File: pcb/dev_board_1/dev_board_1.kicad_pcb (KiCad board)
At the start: 2 copper layers, 90 x 97.5 mm, 54 parts, among them SW1 SW_DIP_x01, SW10 SW_DIP_x01, SW11 SW_DIP_x01, SW12 SW_DIP_x01, SW13 SW_DIP_x01, SW14 SW_DIP_x01, SW15 SW_DIP_x01, SW16 SW_DIP_x01, SW17 SW_DIP_x01, SW18 SW_DIP_x01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

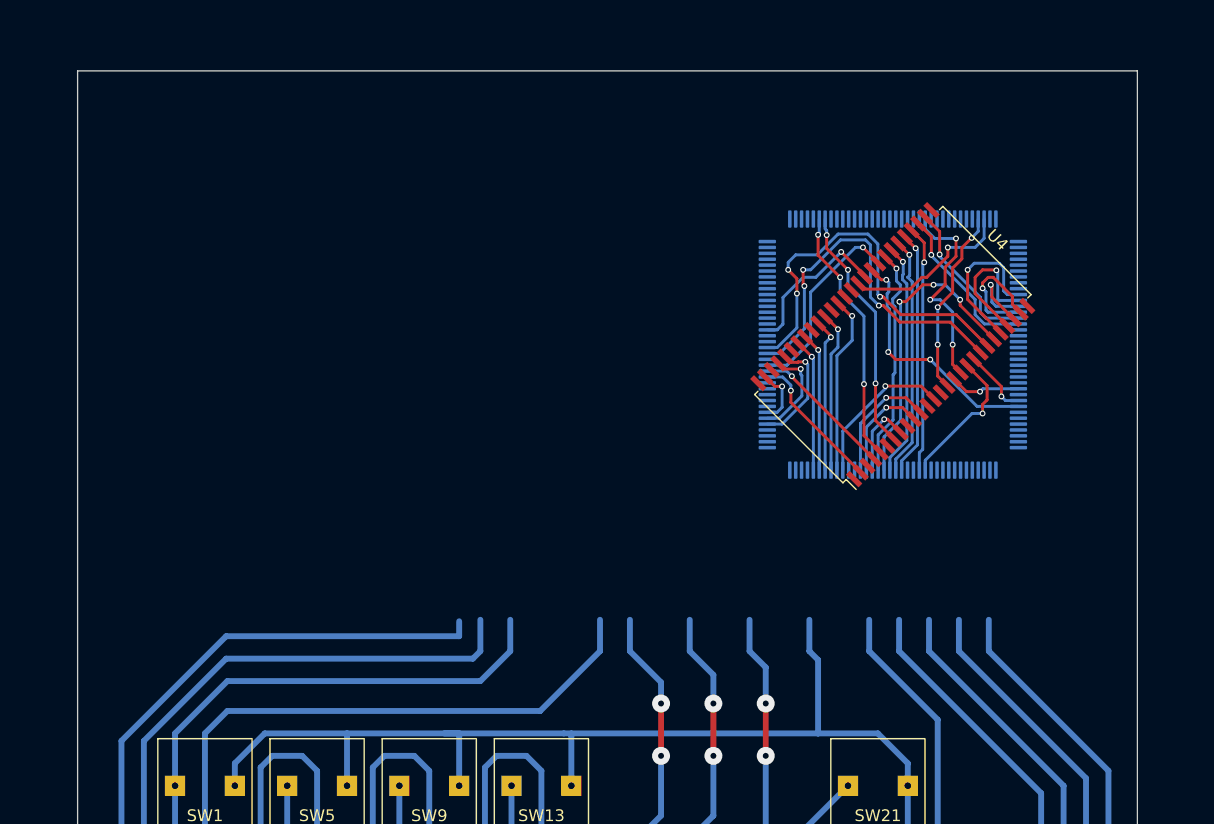
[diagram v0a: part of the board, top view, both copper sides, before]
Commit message: add display
Add ili9341 display whit parallel interface
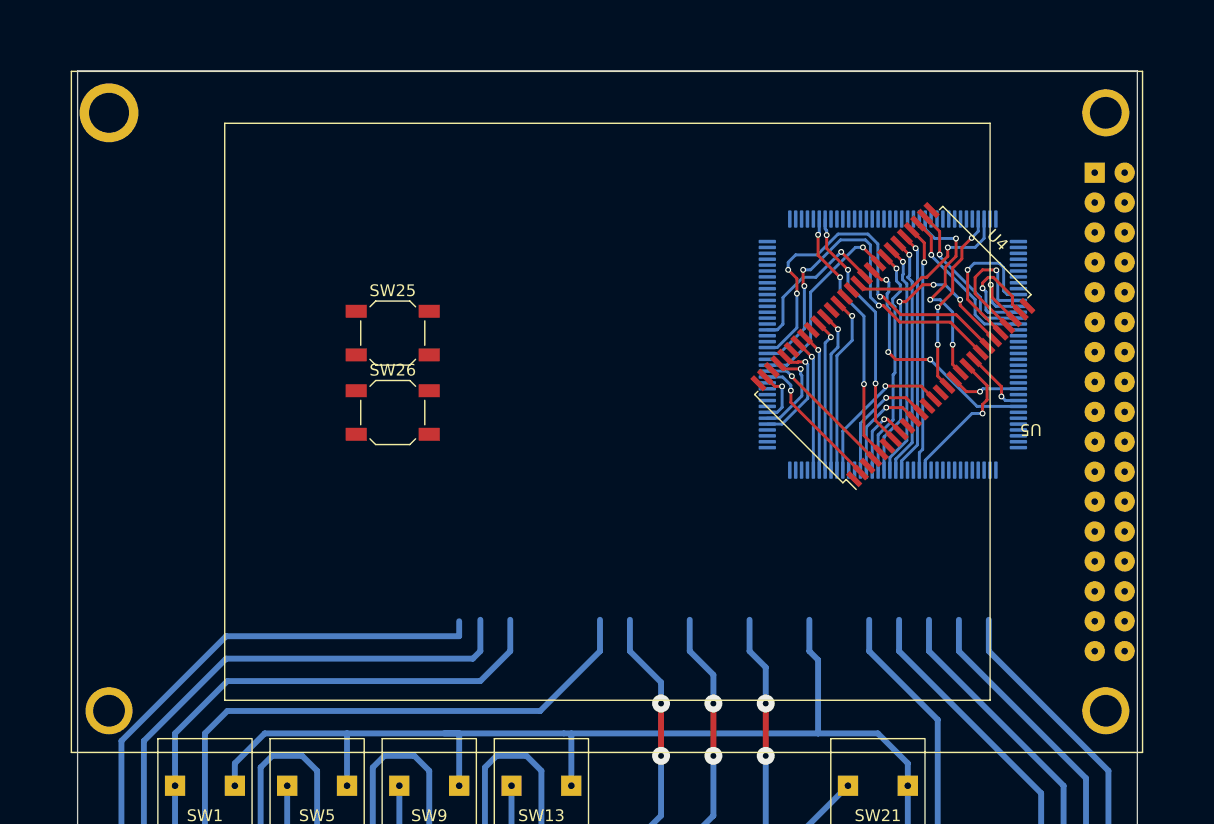
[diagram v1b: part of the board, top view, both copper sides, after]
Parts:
- added SW25: SW_DPST, Button_Switch_SMD:SW_SPST_SKQG_WithStem, F.Cu at (54.6, 41.6)
- added SW26: SW_DPST, Button_Switch_SMD:SW_SPST_SKQG_WithoutStem, F.Cu at (54.6, 48.3)
- added U5: ~, my_lib:ili9486_16bit_3.2, F.Cu at (118.1, 77.1)
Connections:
- net /sdram_A0 renamed /FMC_A0
- net /sdram_A1 renamed /FMC_A1
- net /sdram_A10 renamed /FMC_A10
- net /sdram_A11 renamed /FMC_A11
- net /sdram_A12 renamed /FMC_A12
- net /sdram_A2 renamed /FMC_A2
- net /sdram_A3 renamed /FMC_A3
- net /sdram_A4 renamed /FMC_A4
- net /sdram_A5 renamed /FMC_A5
- net /sdram_A6 renamed /FMC_A6
- net /sdram_A7 renamed /FMC_A7
- net /sdram_A8 renamed /FMC_A8
- net /sdram_A9 renamed /FMC_A9
- net /sdram_BA0 renamed /FMC_BA0
- net /sdram_BA1 renamed /FMC_BA1
- net /sdram_CKE renamed /FMC_CKE
- net /sdram_CLK renamed /FMC_CLK
- net /sdram_D0 renamed /FMC_D0
- net /sdram_D1 renamed /FMC_D1
- net /sdram_D10 renamed /FMC_D10
- net /sdram_D11 renamed /FMC_D11
- net /sdram_D12 renamed /FMC_D12
- net /sdram_D13 renamed /FMC_D13
- net /sdram_D14 renamed /FMC_D14
- net /sdram_D15 renamed /FMC_D15
- net /sdram_D2 renamed /FMC_D2
- net /sdram_D3 renamed /FMC_D3
- net /sdram_D4 renamed /FMC_D4
- net /sdram_D5 renamed /FMC_D5
- net /sdram_D6 renamed /FMC_D6
- net /sdram_D7 renamed /FMC_D7
- net /sdram_D8 renamed /FMC_D8
- net /sdram_D9 renamed /FMC_D9
- net /sdram_DQMH renamed /FMC_DQMH
- net /sdram_DQML renamed /FMC_DQML
- net /sdram_~{CAS} renamed /FMC_~{CAS}
- net /sdram_~{CS} renamed /FMC_~{CS}
- net /sdram_~{RAS} renamed /FMC_~{RAS}
- net /sdram_~{WE} renamed /FMC_~{WE}
- U1 pad 10: sck_touch -> unconnected-(U1-SCK_touch-Pad10)
- U1 pad 11: cs_touch -> unconnected-(U1-~{CS_touch}-Pad11)
- U1 pad 12: mosi_touch -> unconnected-(U1-MOSI_touch-Pad12)
- U1 pad 13: miso_touch -> unconnected-(U1-MISO_touch-Pad13)
- U1 pad 14: irg_touch -> unconnected-(U1-IRQ_touch-Pad14)
- U3 pad 107: Net-(U3-VSS-Pad107) -> GND
- U3 pad 108: unconnected-(U3-VDD-Pad108) -> +3.3V
- U3 pad 118: unconnected-(U3-PD4-Pad118) -> /FMC_NOE
- U3 pad 119: unconnected-(U3-PD5-Pad119) -> /FMC_NWE
- U3 pad 120: Net-(U3-VSS-Pad107) -> GND
- U3 pad 121: unconnected-(U3-VDD-Pad121) -> +3.3V
- U3 pad 123: unconnected-(U3-PD7-Pad123) -> /FMC_NE1
- U3 pad 130: Net-(U3-VSS-Pad107) -> GND
- U3 pad 131: unconnected-(U3-VDD-Pad131) -> +3.3V
- U3 pad 144: unconnected-(U3-VDD-Pad144) -> +3.3V
- U3 pad 16: Net-(U3-VSS-Pad107) -> GND
- U3 pad 17: unconnected-(U3-VDD-Pad17) -> +3.3V
- U3 pad 30: unconnected-(U3-VDD-Pad30) -> +3.3V
- U3 pad 31: unconnected-(U3-VSSA-Pad31) -> GND
- U3 pad 33: unconnected-(U3-VDDA-Pad33) -> +3.3V
- U3 pad 38: Net-(U3-VSS-Pad107) -> GND
- U3 pad 39: unconnected-(U3-VDD-Pad39) -> +3.3V
- U3 pad 51: Net-(U3-VSS-Pad107) -> GND
- U3 pad 52: unconnected-(U3-VDD-Pad52) -> +3.3V
- U3 pad 61: Net-(U3-VSS-Pad107) -> GND
- U3 pad 62: unconnected-(U3-VDD-Pad62) -> +3.3V
- U3 pad 72: unconnected-(U3-VDD-Pad72) -> +3.3V
- U3 pad 80: unconnected-(U3-PD11-Pad80) -> /FMC_A16
- U3 pad 83: Net-(U3-VSS-Pad107) -> GND
- U3 pad 84: unconnected-(U3-VDD-Pad84) -> +3.3V
- U3 pad 94: Net-(U3-VSS-Pad107) -> GND
- U3 pad 95: unconnected-(U3-VDD-Pad95) -> +3.3V
- U4 pad 1: Net-(U4-VDD-Pad1) -> +3.3V
- U4 pad 12: Net-(U4-VSSQ-Pad12) -> GND
- U4 pad 14: Net-(U4-VDD-Pad1) -> +3.3V
- U4 pad 27: Net-(U4-VDD-Pad1) -> +3.3V
- U4 pad 28: Net-(U4-VSS-Pad28) -> GND
- U4 pad 3: Net-(U4-VDDQ-Pad3) -> +3.3V
- U4 pad 41: Net-(U4-VSS-Pad28) -> GND
- U4 pad 43: Net-(U4-VDDQ-Pad3) -> +3.3V
- U4 pad 46: Net-(U4-VSSQ-Pad12) -> GND
- U4 pad 49: Net-(U4-VDDQ-Pad3) -> +3.3V
- U4 pad 52: Net-(U4-VSSQ-Pad12) -> GND
- U4 pad 54: Net-(U4-VSS-Pad28) -> GND
- U4 pad 6: Net-(U4-VSSQ-Pad12) -> GND
- U4 pad 9: Net-(U4-VDDQ-Pad3) -> +3.3V

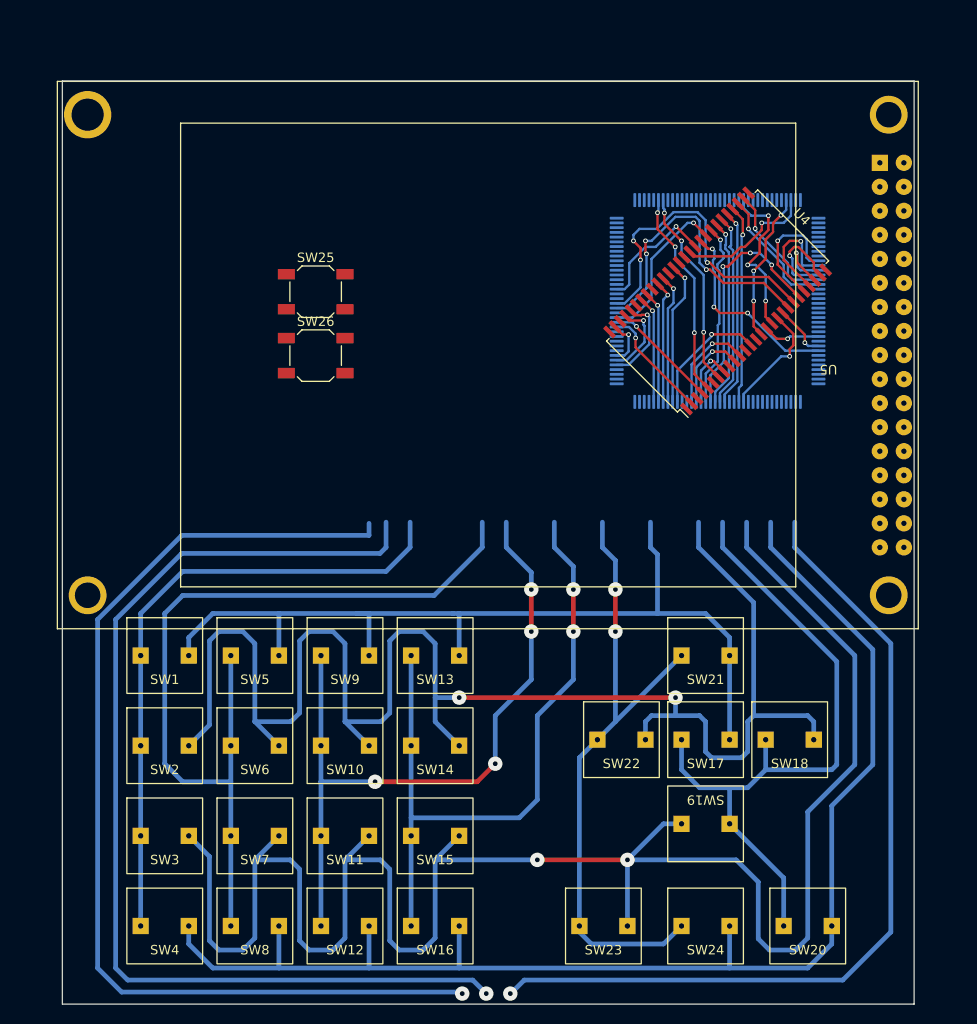
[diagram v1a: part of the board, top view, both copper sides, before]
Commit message: New buttons for calc keyboard
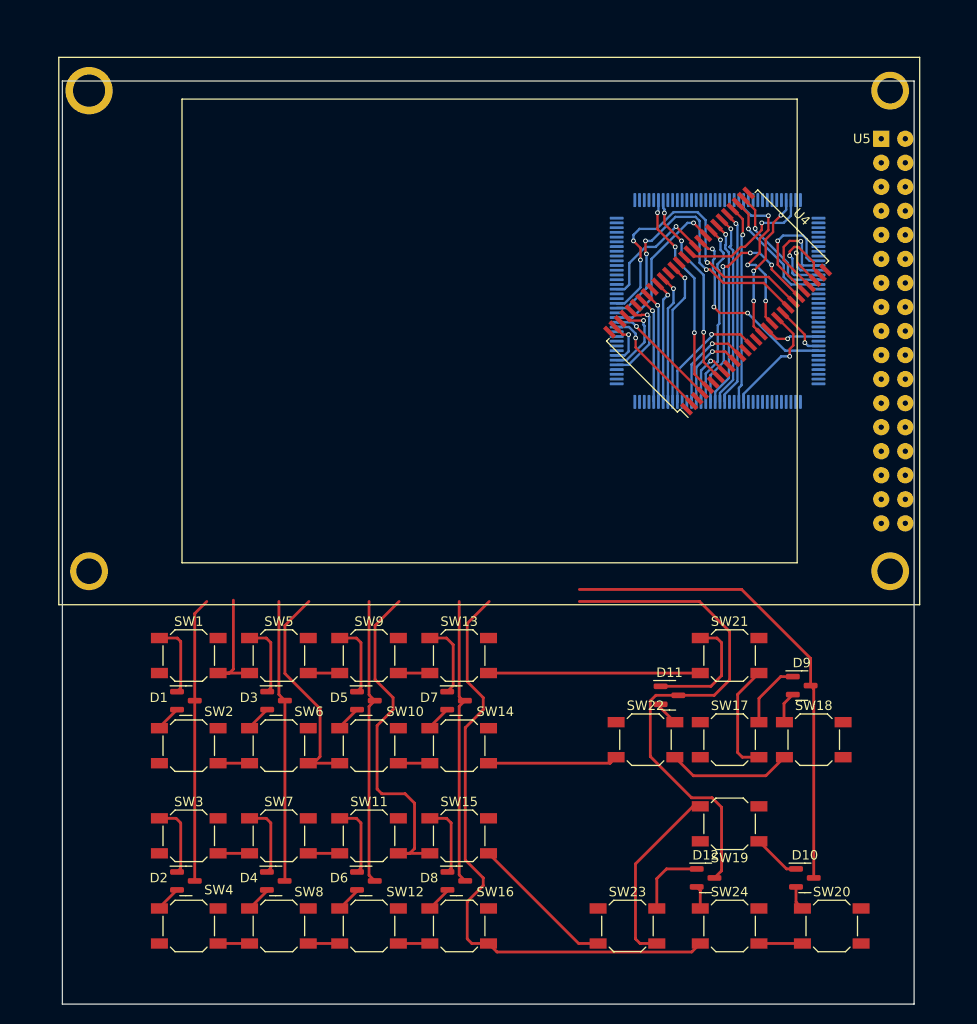
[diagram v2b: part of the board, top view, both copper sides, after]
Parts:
- removed SW25: SW_DPST, Button_Switch_SMD:SW_SPST_SKQG_WithStem
- removed SW26: SW_DPST, Button_Switch_SMD:SW_SPST_SKQG_WithoutStem
- added D1: BAT54C, Package_TO_SOT_SMD:SOT-23, F.Cu at (40.9, 84.8)
- added D10: BAT54C, Package_TO_SOT_SMD:SOT-23, F.Cu at (106.3, 103.5)
- added D11: BAT54C, Package_TO_SOT_SMD:SOT-23, F.Cu at (92.0, 84.2)
- added D12: BAT54C, Package_TO_SOT_SMD:SOT-23, F.Cu at (95.8, 103.5)
- added D2: BAT54C, Package_TO_SOT_SMD:SOT-23, F.Cu at (40.9, 103.8)
- added D3: BAT54C, Package_TO_SOT_SMD:SOT-23, F.Cu at (50.4, 84.8)
- added D4: BAT54C, Package_TO_SOT_SMD:SOT-23, F.Cu at (50.4, 103.8)
- added D5: BAT54C, Package_TO_SOT_SMD:SOT-23, F.Cu at (59.9, 84.8)
- added D6: BAT54C, Package_TO_SOT_SMD:SOT-23, F.Cu at (59.9, 103.8)
- added D7: BAT54C, Package_TO_SOT_SMD:SOT-23, F.Cu at (69.4, 84.8)
- added D8: BAT54C, Package_TO_SOT_SMD:SOT-23, F.Cu at (69.4, 103.8)
- added D9: BAT54C, Package_TO_SOT_SMD:SOT-23, F.Cu at (105.9, 83.2)
- SW1, SW10, SW11, SW12, SW13, SW14, SW15, SW16, SW17, SW18, SW19, SW2, SW20, SW21, SW22, SW23, SW24, SW3, SW4, SW5, SW6, SW7, SW8, SW9: footprint my_lib:btn_8x8 -> Button_Switch_SMD:SW_SPST_SKQG_WithoutStem
- moved SW19 5.08 mm to (98.3, 97.8)
- moved U5 2.54 mm to (118.3, 74.5)
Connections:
- SW1 pad 1: col_1 -> Net-(D1-Pad1)
- SW10 pad 1: col_3 -> Net-(D5-Pad2)
- SW11 pad 1: col_3 -> Net-(D6-Pad1)
- SW12 pad 1: col_3 -> Net-(D6-Pad2)
- SW13 pad 1: col_4 -> Net-(D7-Pad1)
- SW14 pad 1: col_4 -> Net-(D7-Pad2)
- SW15 pad 1: col_4 -> Net-(D8-Pad1)
- SW16 pad 1: col_4 -> Net-(D8-Pad2)
- SW17 pad 1: col_5 -> Net-(D9-Pad1)
- SW18 pad 1: col_5 -> Net-(D9-Pad2)
- SW19 pad 1: col_5 -> Net-(D10-Pad1)
- SW2 pad 1: col_1 -> Net-(D1-Pad2)
- SW20 pad 1: col_5 -> Net-(D10-Pad2)
- SW21 pad 1: col_6 -> Net-(D11-Pad1)
- SW22 pad 1: col_6 -> Net-(D11-Pad2)
- SW23 pad 1: col_6 -> Net-(D12-Pad1)
- SW24 pad 1: col_6 -> Net-(D12-Pad2)
- SW3 pad 1: col_1 -> Net-(D2-Pad1)
- SW4 pad 1: col_1 -> Net-(D2-Pad2)
- SW5 pad 1: col_2 -> Net-(D3-Pad1)
- SW6 pad 1: col_2 -> Net-(D3-Pad2)
- SW7 pad 1: col_2 -> Net-(D4-Pad1)
- SW8 pad 1: col_2 -> Net-(D4-Pad2)
- SW9 pad 1: col_3 -> Net-(D5-Pad1)
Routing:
- net row_3: track 202.5 -> 78.9 mm, vias 2 -> 0
- net row_2: track 169.9 -> 57.5 mm, vias 2 -> 0
- net GND: track 111.8 -> 0.34 mm, vias 1 -> 0
- net +5V: track 109.6 -> 0.00 mm, vias 1 -> 0
- net (no net): track 90.4 -> 0.00 mm, vias 1 -> 0
- net col_2: track 91.3 -> 29.8 mm
- net row_4: track 140.6 -> 79.7 mm
- net col_3: track 76.4 -> 30.3 mm, vias 4 -> 0
- net col_4: track 74.9 -> 30.4 mm, vias 2 -> 0
- net row_1: track 96.5 -> 53.2 mm
- net col_1: track 67.0 -> 30.1 mm
- net col_5: track 72.2 -> 50.8 mm
- net col_6: track 67.9 -> 55.0 mm, vias 2 -> 0
- net Net-(D11-Pad1): track 0.00 -> 12.8 mm
- net Net-(D7-Pad1): track 0.00 -> 7.98 mm
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
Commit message: add another trace for sdram
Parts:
- removed U1: ili9341_touch_3.2, my_lib:ili9341_3.2
- added C18: 100nF, Capacitor_SMD:C_0603_1608Metric_Pad1.08x0.95mm_HandSolder, F.Cu at (95.8, 35.3)
- added C26: 10mkF, Capacitor_SMD:C_0603_1608Metric_Pad1.08x0.95mm_HandSolder, F.Cu at (77.1, 33.1)
- added C27: 100nF, Capacitor_SMD:C_0603_1608Metric_Pad1.08x0.95mm_HandSolder, F.Cu at (95.8, 49.9)
- added C28: 100nF, Capacitor_SMD:C_0603_1608Metric_Pad1.08x0.95mm_HandSolder, F.Cu at (48.6, 50.3)
- added C29: 100nF, Capacitor_SMD:C_0603_1608Metric_Pad1.08x0.95mm_HandSolder, F.Cu at (95.8, 56.2)
- added C30: 100nF, Capacitor_SMD:C_0603_1608Metric_Pad1.08x0.95mm_HandSolder, F.Cu at (49.8, 43.3)
- added C31: 100nF, Capacitor_SMD:C_0603_1608Metric_Pad1.08x0.95mm_HandSolder, F.Cu at (86.9, 33.4)
- added C32: 100nF, Capacitor_SMD:C_0603_1608Metric_Pad1.08x0.95mm_HandSolder, F.Cu at (73.6, 34.8)
- added C33: 100nF, Capacitor_SMD:C_0603_1608Metric_Pad1.08x0.95mm_HandSolder, F.Cu at (87.3, 58.1)
- added C34: 100nF, Capacitor_SMD:C_0603_1608Metric_Pad1.08x0.95mm_HandSolder, F.Cu at (53.9, 58.6)
- added C35: 100nF, Capacitor_SMD:C_0603_1608Metric_Pad1.08x0.95mm_HandSolder, F.Cu at (95.8, 45.7)
- added C36: 100nF, Capacitor_SMD:C_0603_1608Metric_Pad1.08x0.95mm_HandSolder, F.Cu at (61.0, 58.1)
- added C37: 100nF, Capacitor_SMD:C_0603_1608Metric_Pad1.08x0.95mm_HandSolder, F.Cu at (95.8, 54.6)
- added C38: 100nF, Capacitor_SMD:C_0603_1608Metric_Pad1.08x0.95mm_HandSolder, F.Cu at (49.8, 52.7)
- added C39: 100nF, Capacitor_SMD:C_0603_1608Metric_Pad1.08x0.95mm_HandSolder, F.Cu at (52.4, 33.6)
- added C40: 100nF, Capacitor_SMD:C_0603_1608Metric_Pad1.08x0.95mm_HandSolder, F.Cu at (65.3, 32.7)
- added C41: 100nF, Capacitor_SMD:C_0603_1608Metric_Pad1.08x0.95mm_HandSolder, F.Cu at (60.0, 32.7)
- added C42: 100nF, Capacitor_SMD:C_0603_1608Metric_Pad1.08x0.95mm_HandSolder, F.Cu at (76.5, 53.5)
- added C43: 100nF, Capacitor_SMD:C_0603_1608Metric_Pad1.08x0.95mm_HandSolder, F.Cu at (75.6, 42.5)
- added C44: 100nF, Capacitor_SMD:C_0603_1608Metric_Pad1.08x0.95mm_HandSolder, F.Cu at (72.7, 57.7)
- added C45: 100nF, Capacitor_SMD:C_0603_1608Metric_Pad1.08x0.95mm_HandSolder, F.Cu at (65.9, 58.1)
- added U6: STM32F427ZGTx, Package_QFP:LQFP-144_20x20mm_P0.5mm, F.Cu at (62.5, 45.7)
- added U7: MT48LC16M16A2TG, Package_SO:TSOP-II-54_22.2x10.16mm_P0.8mm, F.Cu at (87.3, 45.7)
- moved U5 178.4 mm to (250.8, -44.9)
- moved C15 151.6 mm to (234.7, 52.4)
- moved C16 151.6 mm to (224.5, 51.1)
- moved C17 151.6 mm to (224.5, 53.6)
- moved R1 151.6 mm to (215.3, 53.7)
- moved R2 151.6 mm to (215.3, 50.5)
- moved U2 151.6 mm to (229.9, 53.3)
- moved C25 112.8 mm to (94.9, -73.0)
- moved C19 112.8 mm to (94.3, -88.8)
- moved C20 112.8 mm to (94.3, -86.3)
- moved C21 112.8 mm to (94.3, -83.8)
- moved C22 112.8 mm to (94.3, -81.3)
- moved C23 112.8 mm to (94.3, -78.8)
- moved C24 112.8 mm to (94.3, -76.3)
- moved U3 100.0 mm to (104.5, -57.1)
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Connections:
- U3 pad 23: unconnected-(U3-PH0-Pad23) -> RCC1
- U3 pad 24: unconnected-(U3-PH1-Pad24) -> RCC2
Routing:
- net GND: track 0.34 -> 295.4 mm, vias 0 -> 22
- net +3.3V: track 0.64 -> 279.3 mm
- net /TEST_1_FMC_DQML: track 0.00 -> 57.0 mm, vias 0 -> 2
- net /TEST_1_FMC_~{CAS}: track 0.00 -> 51.6 mm, vias 0 -> 4
- net /TEST_1_FMC_~{WE}: track 0.00 -> 50.6 mm, vias 0 -> 2
- net /TEST_1_FMC_A10: track 0.00 -> 46.8 mm, vias 0 -> 2
- net /TEST_1_FMC_~{CS}: track 0.00 -> 46.0 mm, vias 0 -> 2
- net /TEST_1_FMC_~{RAS}: track 0.00 -> 45.8 mm, vias 0 -> 2
- net /TEST_1_FMC_A3: track 0.00 -> 44.6 mm, vias 0 -> 2
- net /TEST_1_FMC_A2: track 0.00 -> 44.4 mm, vias 0 -> 2
- net /TEST_1_FMC_A1: track 0.00 -> 44.4 mm, vias 0 -> 2
- net /TEST_1_FMC_A0: track 0.00 -> 44.4 mm, vias 0 -> 2
- net /TEST_1_FMC_DQMH: track 0.00 -> 43.1 mm, vias 0 -> 2
- net /TEST_1_FMC_D3: track 0.00 -> 40.3 mm, vias 0 -> 2
- net /TEST_1_FMC_D2: track 0.00 -> 40.0 mm, vias 0 -> 2
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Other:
- board text removed: "30.27 30.48"
